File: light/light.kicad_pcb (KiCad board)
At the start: 2 copper layers, 33 x 69.9 mm, 11 parts, among them J1 Conn_01x03

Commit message: light: Finish scheme and PCB
Signed-off-by: Sam Protsenko <joe.skb7@gmail.com>
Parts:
- J1: value Conn_01x03 -> 4P4C; footprint Connector_PinHeader_2.54mm:PinHeader_1x03_P2.54mm_Horizontal -> Connector_RJ9:RJ9_KLS_12-123-4P
- moved J1 93.3 mm to (56.6, 90.2), turned to 0 degrees
- moved D1 92.5 mm to (45.7, 31.8)
- moved D10 92.5 mm to (61.0, 77.5)
- moved D2 92.5 mm to (61.0, 31.8)
- moved D3 92.5 mm to (53.3, 39.4)
- moved D4 92.5 mm to (45.7, 47.0)
- moved D5 92.5 mm to (61.0, 47.0)
- moved D6 92.5 mm to (45.7, 62.2)
- moved D7 92.5 mm to (61.0, 62.2)
- moved D8 92.5 mm to (53.3, 69.8)
- moved D9 92.5 mm to (45.7, 77.5)
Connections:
- J1 pad 1: Net-(D5-Pad1) -> (no net)
- J1 pad 2: Net-(D10-Pad1) -> Net-(D5-Pad1)
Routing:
- net Net-(D10-Pad1): track 35.1 -> 32.3 mm
- net Net-(D5-Pad1): track 67.4 -> 66.6 mm
- net Net-(D1-Pad2): track 83.9 -> 84.4 mm
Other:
- board size 33 x 69.9 mm -> 33 x 69.8 mm

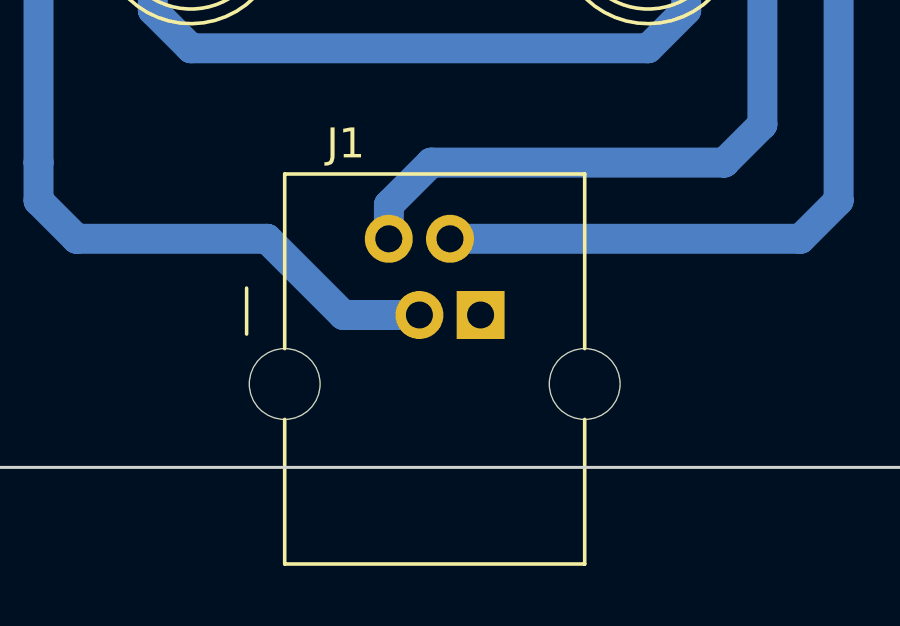
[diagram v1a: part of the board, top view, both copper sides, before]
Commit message: light: Use two pins of RJ9 to pass +12V
Signed-off-by: Sam Protsenko <joe.skb7@gmail.com>
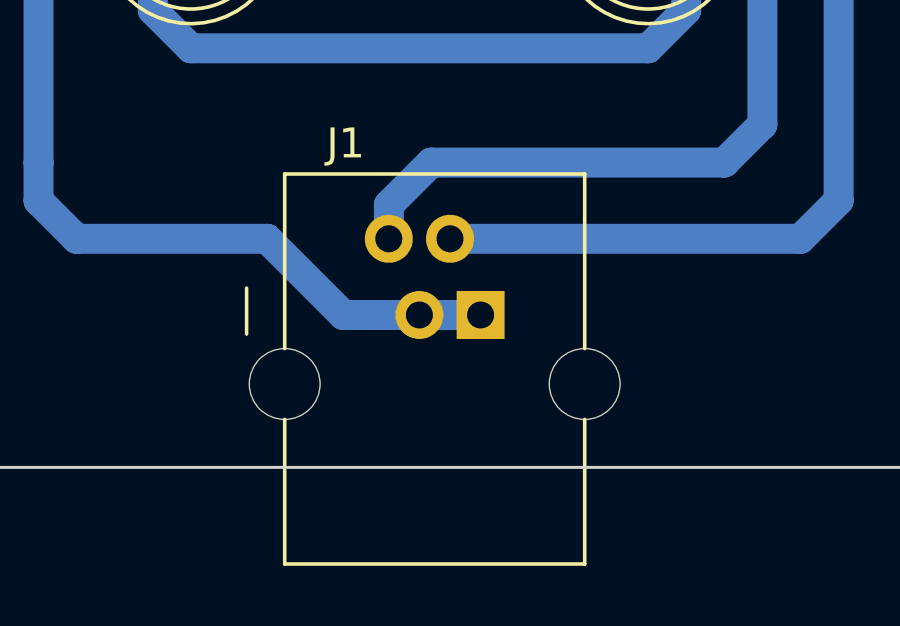
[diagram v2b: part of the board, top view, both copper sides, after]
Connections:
- J1 pad 1: (no net) -> Net-(D1-Pad2)
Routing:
- net Net-(D1-Pad2): track 84.4 -> 86.5 mm
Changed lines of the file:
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@@
-(kicad_pcb (version 20171130) (host pcbnew 5.0.1+dfsg1-3)
+(kicad_pcb (version 20171130) (host pcbnew 5.0.1+dfsg1-3.1)
   (general
     (thickness 1.6)
     (drawings 4)
-    (tracks 62)
+    (tracks 63)
     (zones 0)
     (modules 11)
@@
   )
   (setup
-    (last_trace_width 0.3)
+    (last_trace_width 1)
     (user_trace_width 1)
     (trace_clearance 0.3)
@@
     (pad 2 thru_hole circle (at -1.02 -2.54) (size 1.6 1.6) (drill 0.9) (layers *.Cu *.Mask)
       (net 6 "Net-(D5-Pad1)"))
-    (pad 1 thru_hole rect (at 0 0) (size 1.6 1.6) (drill 0.9) (layers *.Cu *.Mask))
+    (pad 1 thru_hole rect (at 0 0) (size 1.6 1.6) (drill 0.9) (layers *.Cu *.Mask)
+      (net 2 "Net-(D1-Pad2)"))
     (pad "" np_thru_hole circle (at 3.47 2.3) (size 2.36 2.36) (drill 2.36) (layers *.Cu *.Mask))
     (model ${KISYS3DMOD}/Connector_RJ9.3dshapes/RJ9_KLS_12-123-4P.wrl
@@
   (segment (start 41.91 85.09) (end 41.91 67.31) (width 1) (layer B.Cu) (net 2))
   (segment (start 41.91 67.31) (end 41.91 38.1) (width 1) (layer B.Cu) (net 2))
-  (segment (start 54.61 90.17) (end 52.07 90.17) (width 1) (layer B.Cu) (net 2))
+  (segment (start 54.61 90.17) (end 52.07 90.17) (width 1) (layer B.Cu) (net 2) (status 10))
   (segment (start 52.07 90.17) (end 49.53 87.63) (width 1) (layer B.Cu) (net 2))
   (segment (start 49.53 87.63) (end 43.18 87.63) (width 1) (layer B.Cu) (net 2))
   (segment (start 41.91 86.36) (end 41.91 85.09) (width 1) (layer B.Cu) (net 2))
   (segment (start 43.18 87.63) (end 41.91 86.36) (width 1) (layer B.Cu) (net 2))
+  (segment (start 54.606 90.17) (end 56.646 90.17) (width 1) (layer B.Cu) (net 2))
   (segment (start 55.88 39.37) (end 59.69 39.37) (width 1) (layer B.Cu) (net 3) (status 10))
   (segment (start 60.96 38.1) (end 60.96 31.75) (width 1) (layer B.Cu) (net 3) (status 20))
@@
   (segment (start 45.72 49.53) (end 45.72 46.99) (width 1) (layer B.Cu) (net 5) (status 20))
   (segment (start 60.96 44.45) (end 60.96 46.99) (width 1) (layer B.Cu) (net 6) (status 20))
-  (segment (start 55.63 87.63) (end 67.31 87.63) (width 1) (layer B.Cu) (net 6))
+  (segment (start 55.63 87.63) (end 67.31 87.63) (width 1) (layer B.Cu) (net 6) (status 10))
   (segment (start 67.31 87.63) (end 68.58 86.36) (width 1) (layer B.Cu) (net 6))
   (segment (start 68.58 86.36) (end 68.58 44.45) (width 1) (layer B.Cu) (net 6))
@@
   (segment (start 60.96 74.93) (end 62.23 73.66) (width 1) (layer B.Cu) (net 11))
   (segment (start 53.59 86.49863) (end 54.99863 85.09) (width 1) (layer B.Cu) (net 11))
-  (segment (start 53.59 87.63) (end 53.59 86.49863) (width 1) (layer B.Cu) (net 11))
+  (segment (start 53.59 87.63) (end 53.59 86.49863) (width 1) (layer B.Cu) (net 11) (status 10))
   (segment (start 54.99863 85.09) (end 64.77 85.09) (width 1) (layer B.Cu) (net 11))
   (segment (start 66.04 83.82) (end 66.04 74.93) (width 1) (layer B.Cu) (net 11))
